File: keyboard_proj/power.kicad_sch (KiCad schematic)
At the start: 16 parts

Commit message: Tous les schematics vérifiés 1x
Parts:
- added IC?: USBLC6-4SC6, SOT95P280X145-6N, symbol SamacSys_Parts:USBLC6-2SC6
- added U?: 918-418K2023S40026, symbol My_lib:918-418K2023S40026
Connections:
- net GND: now also IC?.2 (GND), U?.1 (GND), U?.10 (SHELL), U?.6 (GND), U?.7 (SHELL), U?.8 (SHELL), U?.9 (SHELL)
- net VDDUSB: no longer C?.1
- net 1.8V renamed 3.3V
- new net: IC?.1 (I/O1_1), U?.3 (CC1)
- new net: IC?.3 (I/O2_1), U?.4 (CC2)
- new net D+: IC?.6 (I/O1_2)
- new net D-: IC?.4 (I/O2_2)
- new net VBUS: C?.1, IC?.5 (VBUS), U?.2 (VBUS), U?.5 (VBUS)
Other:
- note added: "ESD protection"
- moved on the sheet: C?

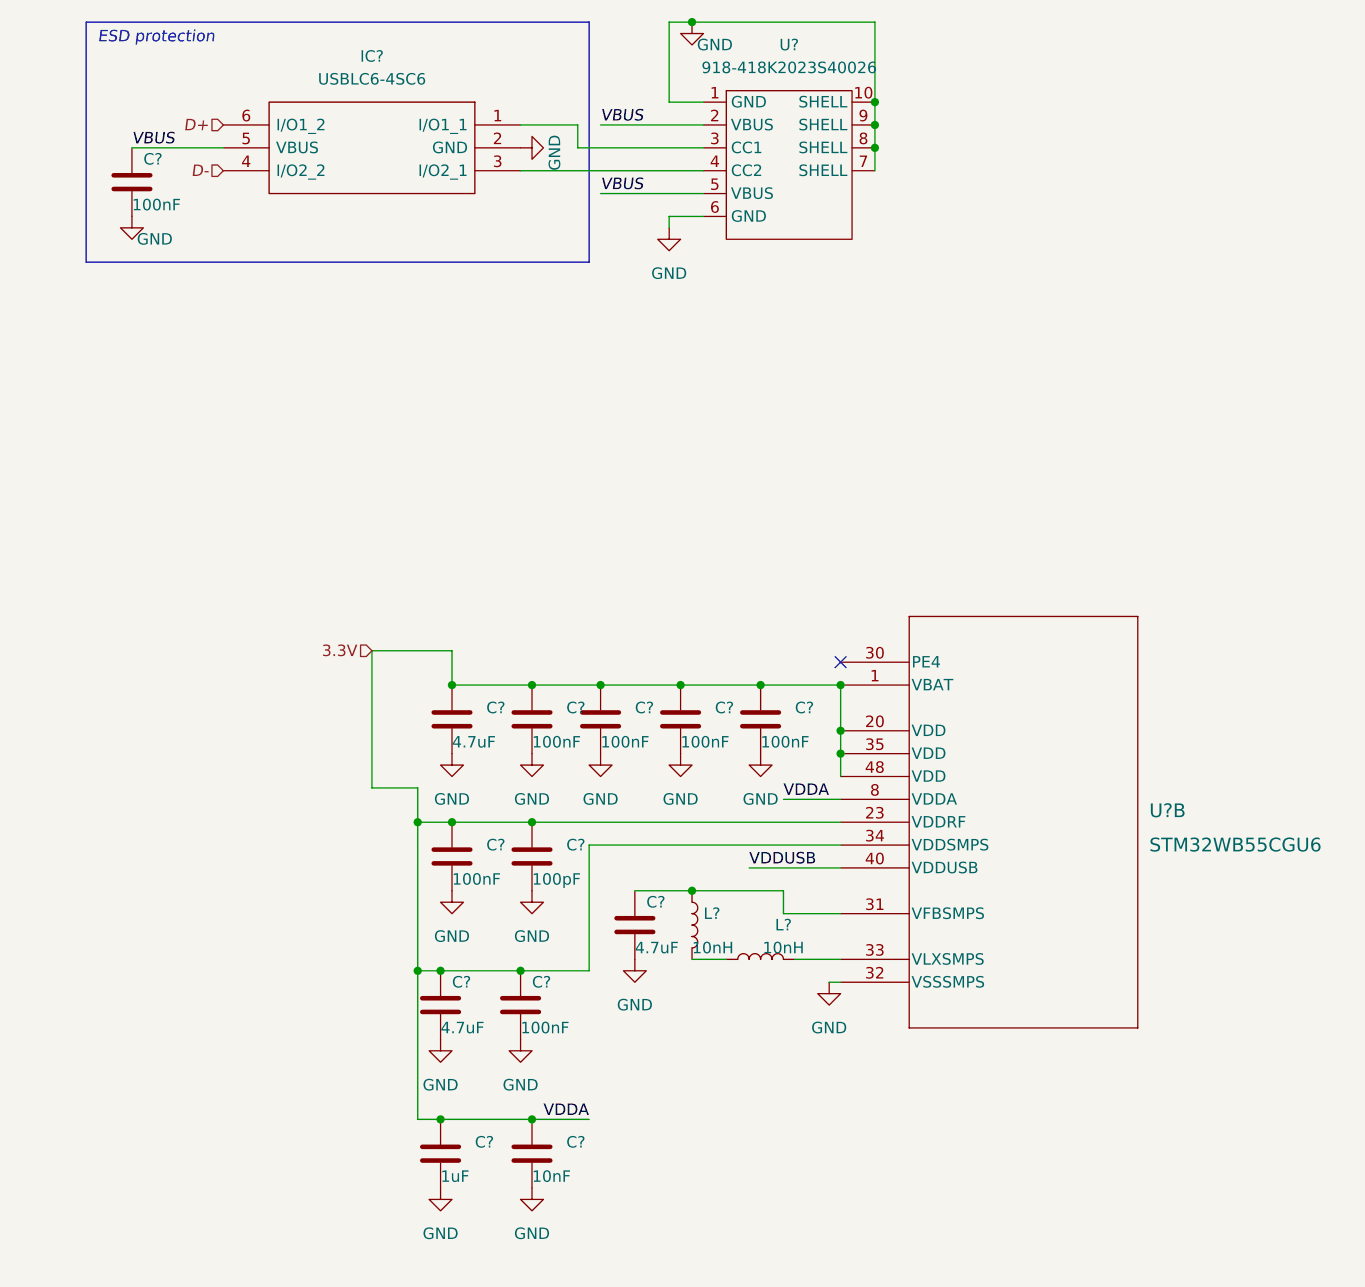
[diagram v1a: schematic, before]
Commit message: Ajout backlight et light sensor (in progress)
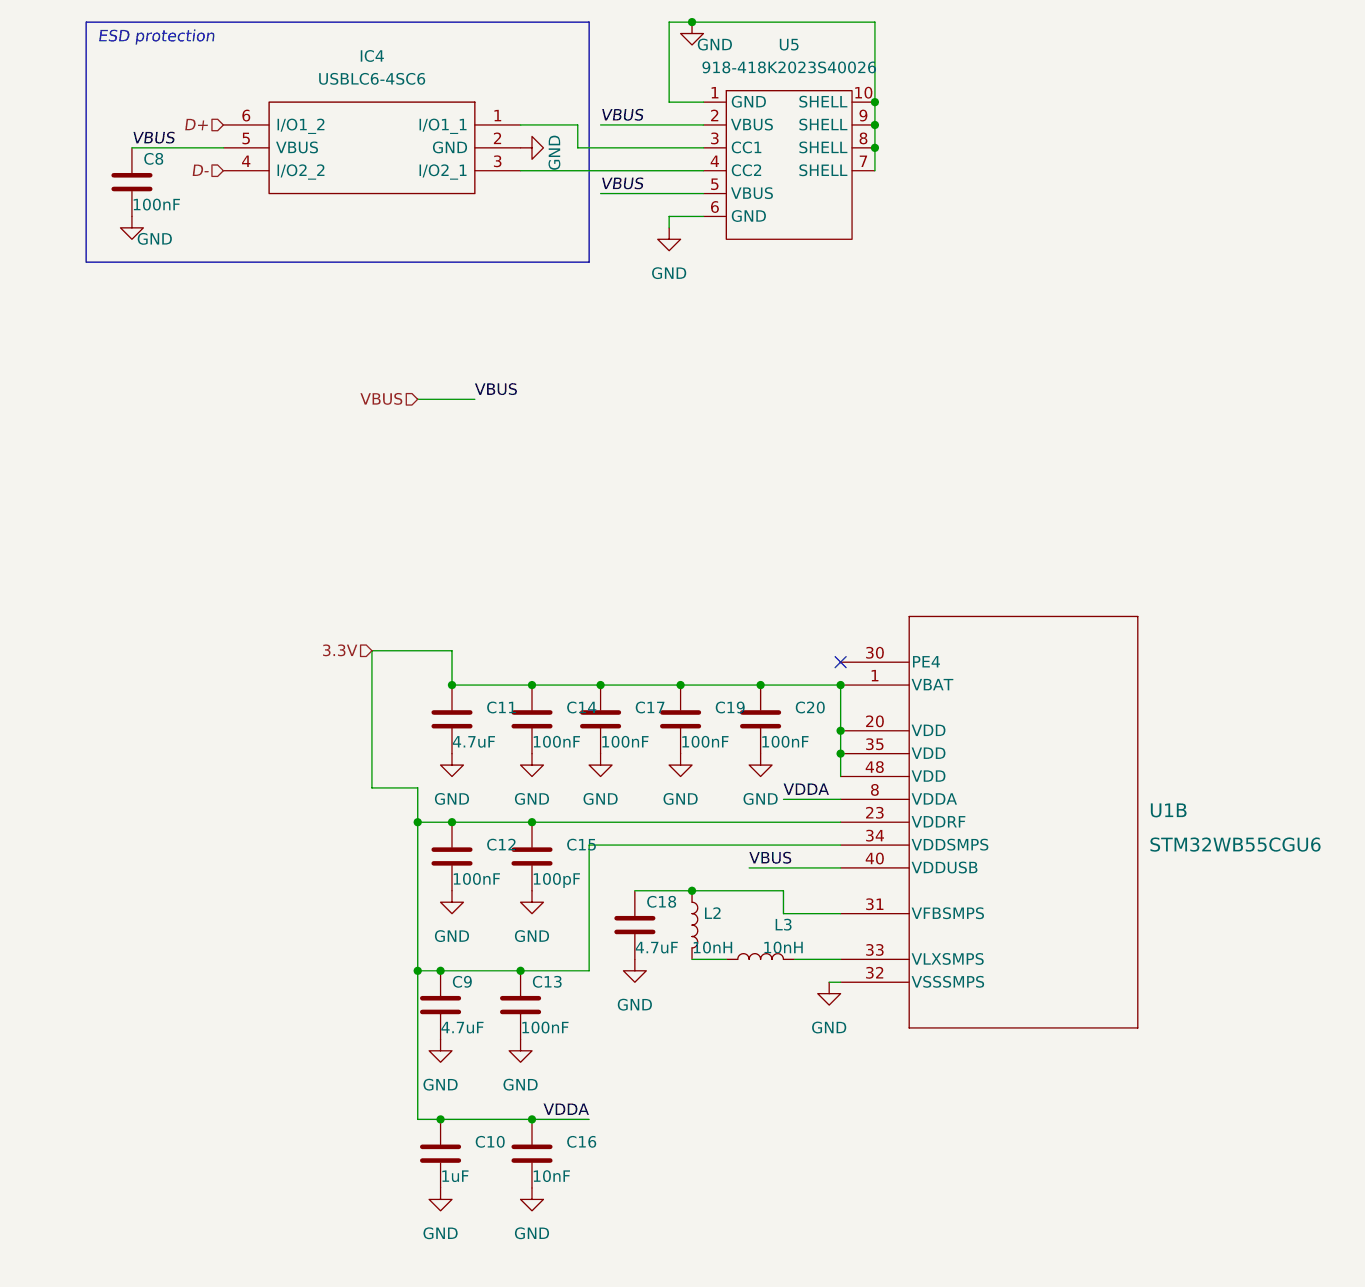
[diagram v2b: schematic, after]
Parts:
- gave numbers to parts that had none: 18
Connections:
- net VDDUSB is gone; now on net VBUS: U1.40 (VDDUSB)

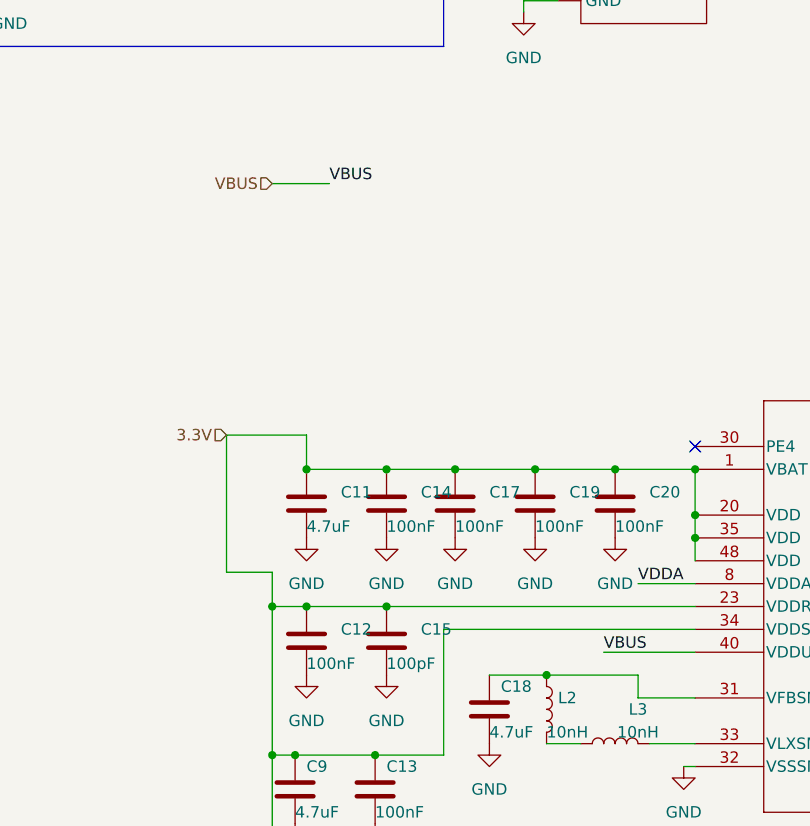
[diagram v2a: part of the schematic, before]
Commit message: Ajout light sensor et controle avec mosfet pour backlight
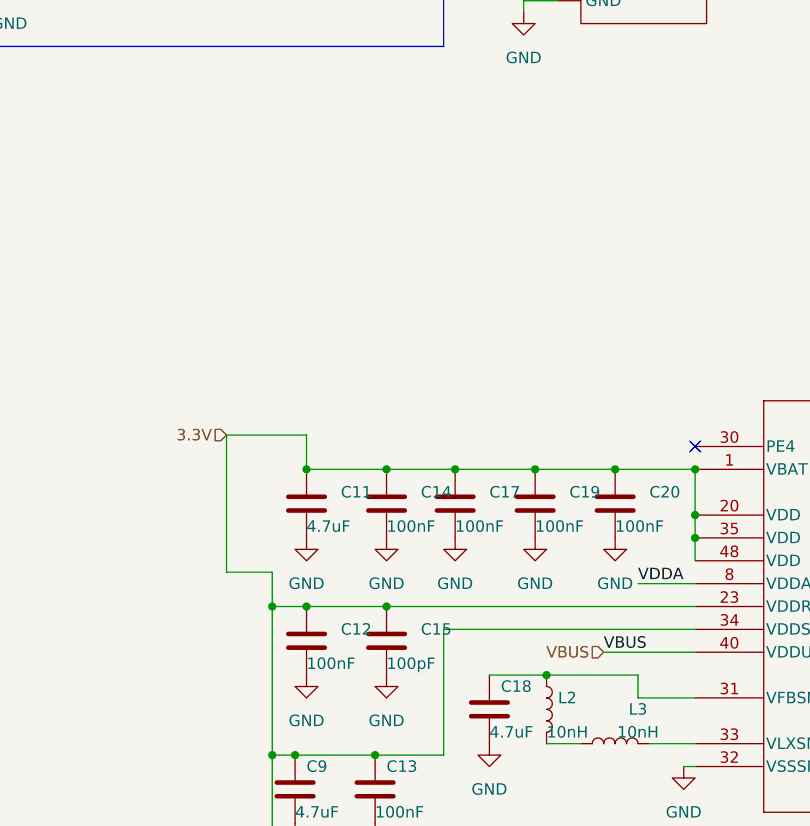
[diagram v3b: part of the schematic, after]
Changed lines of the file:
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@@
-    (stroke (width 0) (type default) (color 0 0 0 0))
-  )
-  (wire (pts (xy 83.82 76.2) (xy 90.17 76.2))
     (stroke (width 0) (type default) (color 0 0 0 0))
   )
@@
     (effects (font (size 1.27 1.27)) (justify left bottom))
   )
-  (label "VBUS" (at 90.17 76.2 0)
-    (effects (font (size 1.27 1.27)) (justify left bottom))
-  )
   (label "VDDA" (at 124.46 120.65 0)
     (effects (font (size 1.27 1.27)) (justify left bottom))
@@
     (effects (font (size 1.27 1.27) italic) (justify right))
   )
+  (hierarchical_label "VBUS" (shape input) (at 120.65 128.27 180)
+    (effects (font (size 1.27 1.27)) (justify right))
+  )
   (hierarchical_label "3.3V" (shape input) (at 78.74 104.14 180)
     (effects (font (size 1.27 1.27)) (justify right))
   )
-  (hierarchical_label "VBUS" (shape input) (at 83.82 76.2 180)
-    (effects (font (size 1.27 1.27)) (justify right))
-  )

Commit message: Ajout des empreintes, il en manque encore
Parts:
- C10, C11, C12, C13, C14, C15, C16, C17, C18, C19, C20, C8, C9: footprint (none) -> Capacitor_SMD:C_0402_1005Metric
- IC4: footprint SOT95P280X145-6N -> (none)
- L2, L3: footprint (none) -> Inductor_SMD:L_0402_1005Metric
- U1: footprint UFQFPN48-7x7mm -> STM32WB:UFQFPN48-7x7mm
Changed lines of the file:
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@@
       (effects (font (size 1.27 1.27)) (justify left))
     )
-    (property "Footprint" "" (id 2) (at 53.0352 55.88 0)
+    (property "Footprint" "Capacitor_SMD:C_0402_1005Metric" (id 2) (at 53.0352 55.88 0)
       (effects (font (size 1.27 1.27)) hide)
     )
@@
       (effects (font (size 1.27 1.27)) (justify left))
     )
-    (property "Footprint" "" (id 2) (at 96.2152 147.32 0)
+    (property "Footprint" "Capacitor_SMD:C_0402_1005Metric" (id 2) (at 96.2152 147.32 0)
       (effects (font (size 1.27 1.27)) hide)
     )
@@
       (effects (font (size 1.27 1.27)) (justify left))
     )
-    (property "Footprint" "" (id 2) (at 122.8852 115.57 0)
+    (property "Footprint" "Capacitor_SMD:C_0402_1005Metric" (id 2) (at 122.8852 115.57 0)
       (effects (font (size 1.27 1.27)) hide)
     )
@@
       (effects (font (size 1.27 1.27)) (justify left))
     )
-    (property "Footprint" "" (id 2) (at 97.4852 130.81 0)
+    (property "Footprint" "Capacitor_SMD:C_0402_1005Metric" (id 2) (at 97.4852 130.81 0)
       (effects (font (size 1.27 1.27)) hide)
     )
@@
       (effects (font (size 1.27 1.27)) (justify left))
     )
-    (property "Footprint" "" (id 2) (at 97.4852 163.83 0)
+    (property "Footprint" "Capacitor_SMD:C_0402_1005Metric" (id 2) (at 97.4852 163.83 0)
       (effects (font (size 1.27 1.27)) hide)
     )
@@
     (property "Reference" "IC4" (id 0) (at 78.74 38.1 0))
     (property "Value" "USBLC6-4SC6" (id 1) (at 78.74 40.64 0))
-    (property "Footprint" "SOT95P280X145-6N" (id 2) (at 66.04 43.18 0)
+    (property "Footprint" "" (id 2) (at 66.04 43.18 0)
       (effects (font (size 1.27 1.27)) (justify left) hide)
     )
@@
       (effects (font (size 1.27 1.27)) (justify left))
     )
-    (property "Footprint" "" (id 2) (at 114.3 134.62 0)
+    (property "Footprint" "Inductor_SMD:L_0402_1005Metric" (id 2) (at 114.3 134.62 0)
       (effects (font (size 1.27 1.27)) hide)
     )
@@
       (effects (font (size 1.27 1.27)) (justify left))
     )
-    (property "Footprint" "" (id 2) (at 108.9152 138.43 0)
+    (property "Footprint" "Capacitor_SMD:C_0402_1005Metric" (id 2) (at 108.9152 138.43 0)
       (effects (font (size 1.27 1.27)) hide)
     )
@@
       (effects (font (size 1.27 1.27)) (justify left))
     )
-    (property "Footprint" "" (id 2) (at 105.1052 115.57 0)
+    (property "Footprint" "Capacitor_SMD:C_0402_1005Metric" (id 2) (at 105.1052 115.57 0)
       (effects (font (size 1.27 1.27)) hide)
     )
@@
       (effects (font (size 1.27 1.27)) (justify left))
     )
-    (property "Footprint" "" (id 2) (at 88.5952 115.57 0)
+    (property "Footprint" "Capacitor_SMD:C_0402_1005Metric" (id 2) (at 88.5952 115.57 0)
       (effects (font (size 1.27 1.27)) hide)
     )
@@
       (effects (font (size 1.524 1.524)) (justify left))
     )
-    (property "Footprint" "UFQFPN48-7x7mm" (id 2) (at 130.81 105.41 0)
+    (property "Footprint" "STM32WB:UFQFPN48-7x7mm" (id 2) (at 130.81 105.41 0)
       (effects (font (size 1.27 1.27) italic) hide)
     )
@@
       (effects (font (size 1.27 1.27)) (justify left))
     )
-    (property "Footprint" "" (id 2) (at 88.5952 130.81 0)
+    (property "Footprint" "Capacitor_SMD:C_0402_1005Metric" (id 2) (at 88.5952 130.81 0)
       (effects (font (size 1.27 1.27)) hide)
     )
@@
     (property "Reference" "L3" (id 0) (at 124.46 134.62 90))
     (property "Value" "10nH" (id 1) (at 124.46 137.16 90))
-    (property "Footprint" "" (id 2) (at 121.92 138.43 0)
+    (property "Footprint" "Inductor_SMD:L_0402_1005Metric" (id 2) (at 121.92 138.43 0)
       (effects (font (size 1.27 1.27)) hide)
     )
@@
       (effects (font (size 1.27 1.27)) (justify left))
     )
-    (property "Footprint" "" (id 2) (at 87.3252 147.32 0)
+    (property "Footprint" "Capacitor_SMD:C_0402_1005Metric" (id 2) (at 87.3252 147.32 0)
       (effects (font (size 1.27 1.27)) hide)
     )
@@
       (effects (font (size 1.27 1.27)) (justify left))
     )
-    (property "Footprint" "" (id 2) (at 97.4852 115.57 0)
+    (property "Footprint" "Capacitor_SMD:C_0402_1005Metric" (id 2) (at 97.4852 115.57 0)
       (effects (font (size 1.27 1.27)) hide)
     )
@@
       (effects (font (size 1.27 1.27)) (justify left))
     )
-    (property "Footprint" "" (id 2) (at 87.3252 163.83 0)
+    (property "Footprint" "Capacitor_SMD:C_0402_1005Metric" (id 2) (at 87.3252 163.83 0)
       (effects (font (size 1.27 1.27)) hide)
     )
@@
       (effects (font (size 1.27 1.27)) (justify left))
     )
-    (property "Footprint" "" (id 2) (at 113.9952 115.57 0)
-      (effects (font (size 1.27 1.27)) hide)
-    )
+    (property "Footprint" "Capacitor_SMD:C_0402_1005Metric" (id 2) (at 113.9952 115.57 0)
+      (effects (font (size 1.27 1.27)) hide)
+    )

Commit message: Empreintes finies, besoin de reverifier, disposition des composants sur la carte
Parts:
- IC4: footprint (none) -> SamacSys_Parts:SOT95P280X145-6N
- U5: footprint (none) -> SamacSys_Parts:USB_conn
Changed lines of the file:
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@@
     (property "Reference" "IC4" (id 0) (at 78.74 38.1 0))
     (property "Value" "USBLC6-4SC6" (id 1) (at 78.74 40.64 0))
-    (property "Footprint" "" (id 2) (at 66.04 43.18 0)
+    (property "Footprint" "SamacSys_Parts:SOT95P280X145-6N" (id 2) (at 66.04 43.18 0)
       (effects (font (size 1.27 1.27)) (justify left) hide)
     )
@@
     (property "Reference" "U5" (id 0) (at 125.095 36.83 0))
     (property "Value" "918-418K2023S40026" (id 1) (at 125.095 39.37 0))
-    (property "Footprint" "" (id 2) (at 121.92 45.72 0)
-      (effects (font (size 1.27 1.27)) hide)
-    )
+    (property "Footprint" "SamacSys_Parts:USB_conn" (id 2) (at 121.92 45.72 0)
+      (effects (font (size 1.27 1.27)) hide)
+    )
